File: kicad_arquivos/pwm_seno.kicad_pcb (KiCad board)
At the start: 2 copper layers, 0 parts

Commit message: Finalizado roteamento, gerados gerbers e BOM, adicionado esquematico PDF
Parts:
- added C1: 2200u, Capacitor_THT:CP_Radial_D24.0mm_P10.00mm_SnapIn, F.Cu at (87.6, 47.6)
- added C2: 2200u, Capacitor_THT:CP_Radial_D24.0mm_P10.00mm_SnapIn, F.Cu at (87.6, 88.5)
- added C4: 33u, Capacitor_THT:CP_Radial_D8.0mm_P3.80mm, F.Cu at (139.2, 77.2)
- added H1: MountingHole, MountingHole:MountingHole_3.2mm_M3, F.Cu at (27.4, 26.4)
- added H2: MountingHole, MountingHole:MountingHole_3.2mm_M3, F.Cu at (161.5, 26.4)
- added H3: MountingHole, MountingHole:MountingHole_3.2mm_M3, F.Cu at (27.4, 107.7)
- added H4: MountingHole, MountingHole:MountingHole_3.2mm_M3, F.Cu at (161.5, 107.7)
- added J1: PWR, TerminalBlock:TerminalBlock_bornier-2_P5.08mm, F.Cu at (33.0, 62.2)
- added J2: CTRL, TerminalBlock:TerminalBlock_bornier-3_P5.08mm, F.Cu at (33.0, 88.9)
- added LS1: Speaker, TerminalBlock:TerminalBlock_bornier-2_P5.08mm, F.Cu at (160.5, 65.5)
- added Q1: BC337, Package_TO_SOT_THT:TO-92_Inline_Wide, F.Cu at (67.3, 52.5)
- added Q2: BC337, Package_TO_SOT_THT:TO-92_Inline_Wide, F.Cu at (76.2, 52.5)
- added Q3: BC337, Package_TO_SOT_THT:TO-92_Inline_Wide, F.Cu at (67.3, 78.3)
- added Q4: BC337, Package_TO_SOT_THT:TO-92_Inline_Wide, F.Cu at (76.2, 78.3)
- added Q5: IRF9540N, Package_TO_SOT_THT:TO-220-3_Vertical, F.Cu at (106.7, 28.9)
- added Q6: IRF540N, Package_TO_SOT_THT:TO-220-3_Vertical, F.Cu at (111.8, 107.2)
- added Q7: IRF9540N, Package_TO_SOT_THT:TO-220-3_Vertical, F.Cu at (148.8, 28.9)
- added Q8: IRF540N, Package_TO_SOT_THT:TO-220-3_Vertical, F.Cu at (153.9, 107.2)
- added R1: 3.3K, Resistor_THT:R_Axial_DIN0207_L6.3mm_D2.5mm_P10.16mm_Horizontal, F.Cu at (67.3, 46.6)
- added R2: 150R, Resistor_THT:R_Axial_DIN0414_L11.9mm_D4.5mm_P20.32mm_Horizontal, F.Cu at (61.0, 36.8)
- added R3: 10K, Resistor_THT:R_Axial_DIN0207_L6.3mm_D2.5mm_P10.16mm_Horizontal, F.Cu at (71.8, 36.4)
- added R4: 150R, Resistor_THT:R_Axial_DIN0414_L11.9mm_D4.5mm_P20.32mm_Horizontal, F.Cu at (53.3, 36.8)
- added R5: 3.3K, Resistor_THT:R_Axial_DIN0207_L6.3mm_D2.5mm_P10.16mm_Horizontal, F.Cu at (67.3, 99.5)
- added R6: 150R, Resistor_THT:R_Axial_DIN0414_L11.9mm_D4.5mm_P20.32mm_Horizontal, F.Cu at (61.0, 99.1)
- added R7: 10K, Resistor_THT:R_Axial_DIN0207_L6.3mm_D2.5mm_P10.16mm_Horizontal, F.Cu at (72.4, 99.5)
- added R8: 150R, Resistor_THT:R_Axial_DIN0414_L11.9mm_D4.5mm_P20.32mm_Horizontal, F.Cu at (53.3, 99.1)
- added R9: 1R, Resistor_THT:R_Axial_DIN0922_L20.0mm_D9.0mm_P30.48mm_Horizontal, F.Cu at (139.7, 66.5)
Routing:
- net VCC: track 0.00 -> 281.7 mm
- net /PFET2: track 0.00 -> 173.5 mm, vias 0 -> 2
- net /NFET2: track 0.00 -> 151.2 mm, vias 0 -> 4
- net /PFET1: track 0.00 -> 137.3 mm
- net /L2: track 0.00 -> 117.9 mm
- net /NFET1: track 0.00 -> 85.7 mm
- net /L1: track 0.00 -> 79.3 mm
- net /PWM1: track 0.00 -> 73.8 mm
- net /PWM2: track 0.00 -> 36.6 mm
- net Net-(C4-Pad1): track 0.00 -> 33.4 mm
- net Net-(Q1-Pad2): track 0.00 -> 29.7 mm
- net Net-(Q4-Pad2): track 0.00 -> 24.1 mm
- net Net-(Q2-Pad2): track 0.00 -> 23.1 mm
- net Net-(Q3-Pad2): track 0.00 -> 21.2 mm
- added copper zone on B.Cu, net GND
- added copper zone on F.Cu, net GND
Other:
- board outline added: 142.2 x 89.4 mm
- net class Default: clearance 0.2 -> 0.3; trace_width 0.25 -> 1; via_dia 0.8 -> 2; via_drill 0.4 -> 0.8
- net class Load added: clearance 0.3, trace_width 2, via_dia 2, via_drill 0.8
- net class PWR added: clearance 0.3, trace_width 2, via_dia 2, via_drill 0.8
- net class Sig added: clearance 0.3, trace_width 0.8, via_dia 2, via_drill 0.8
- rule trace_clearance: 0.2 -> 0.3

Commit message: Adicionado segundo filtro
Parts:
- added C4: CP, Capacitor_THT:CP_Radial_D8.0mm_P3.80mm, F.Cu at (147.8, 85.3)
- added R10: 1R, Resistor_THT:R_Axial_DIN0922_L20.0mm_D9.0mm_P30.48mm_Horizontal, F.Cu at (147.8, 76.7)
- moved C5 13.1 mm to (147.8, 67.3), turned to 90 degrees
- renumbered C4 to C5
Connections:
- C5 pad 1: Net-(C4-Pad1) -> Net-(C5-Pad1)
- LS1 pad 2: Net-(C4-Pad1) -> Net-(C5-Pad1)
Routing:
- net Net-(C4-Pad1): track 33.4 -> 72.9 mm
- net Net-(C5-Pad1): track 0.00 -> 28.0 mm
- net /L2: track 117.9 -> 112.5 mm

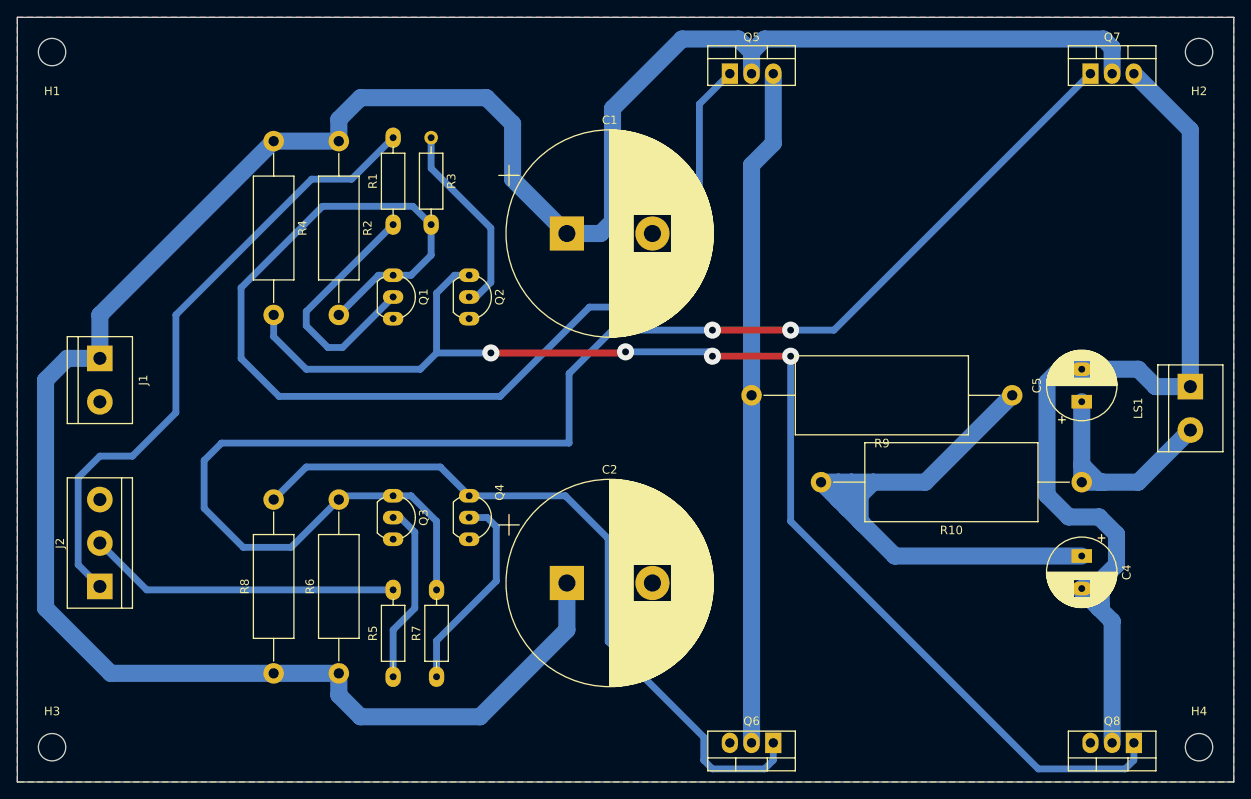
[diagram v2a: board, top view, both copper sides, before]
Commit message: Adicionada segunda ordem ao filtro
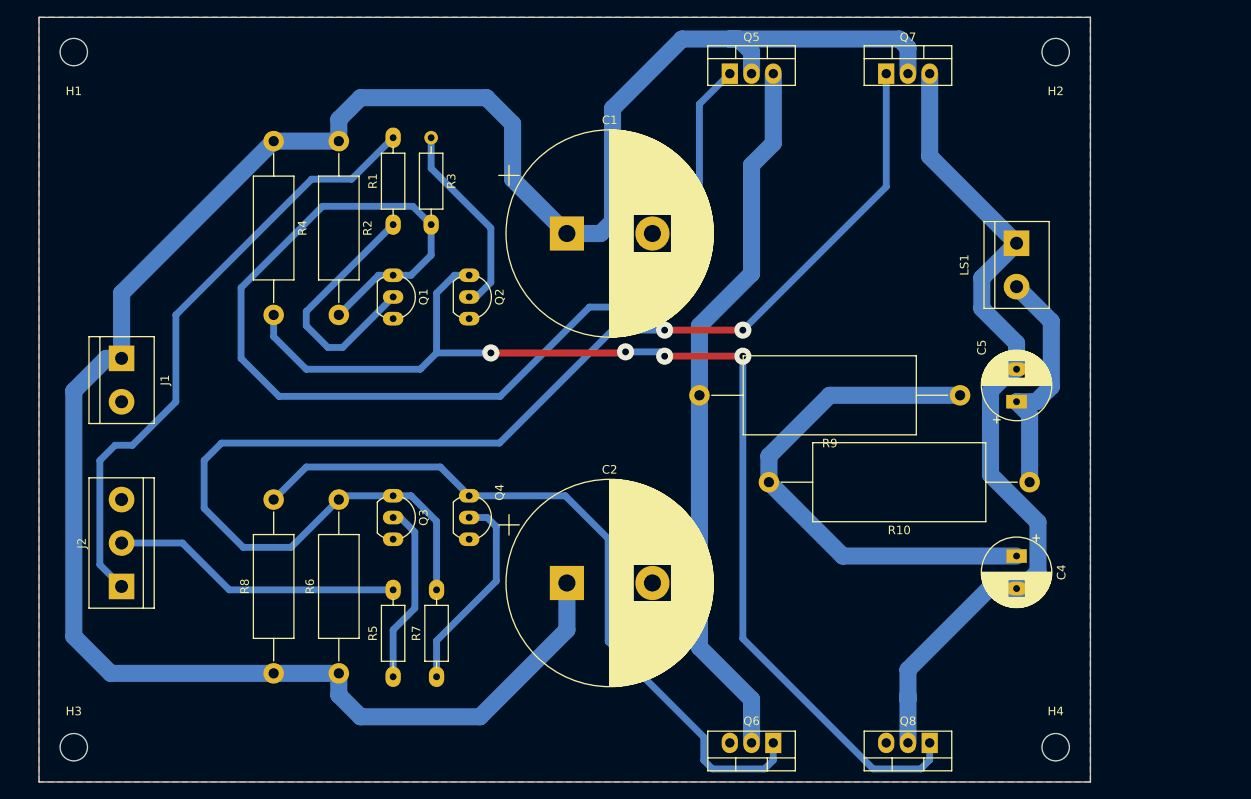
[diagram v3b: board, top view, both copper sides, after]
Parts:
- moved LS1 26.3 mm to (140.2, 48.8)
- moved Q8 23.9 mm to (130.0, 107.2)
- moved Q7 23.9 mm to (125.0, 28.9)
- moved H2 16.8 mm to (144.8, 26.4)
- moved H4 16.8 mm to (144.8, 107.7)
- moved C4 7.62 mm to (140.2, 85.3)
- moved C5 7.62 mm to (140.2, 67.3)
- moved R10 6.10 mm to (141.7, 76.7)
- moved R9 6.10 mm to (133.6, 66.5)
- moved H1 2.54 mm to (30.0, 26.4)
- moved H3 2.54 mm to (30.0, 107.7)
- moved J1 2.54 mm to (35.6, 62.2)
- moved J2 2.54 mm to (35.6, 88.9)
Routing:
- net VCC: track 281.7 -> 255.8 mm
- net /PFET2: track 173.5 -> 152.6 mm
- net /NFET2: track 151.2 -> 135.3 mm
- net /L2: track 112.5 -> 98.7 mm
- net Net-(C4-Pad1): track 72.9 -> 60.9 mm
- net /L1: track 79.3 -> 84.4 mm
- net /PWM2: track 36.6 -> 34.0 mm
- net /PWM1: track 73.8 -> 71.7 mm
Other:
- board size 142.2 x 89.4 mm -> 122.9 x 89.4 mm
